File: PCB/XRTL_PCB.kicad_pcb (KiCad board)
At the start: 2 copper layers, 94 x 78.7 mm, 20 parts, among them J1 POWER, J10 servo1, J11 servo2, J12 infoLED, J2 stepper1, J3 stepper2, J4 ESP32 right, J5 ESP32 left, J6 relay1 IN, J7 relay2 IN, J8 relay1 OUT, J9 relay2 OUT, K1 TIANBO-HJR-4102-L, K2 TIANBO-HJR-4102-L, U1 TBD62003, U2 TBD62003

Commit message: Add files via upload
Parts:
- J6: value relay1 IN -> relay2 IN
- J7: value relay2 IN -> relay1 IN
- J8: value relay1 OUT -> relay2 OUT
- J9: value relay2 OUT -> relay1 OUT
- moved J11 90.9 mm to (132.1, 71.1), turned to 0 degrees
- moved J4 82.9 mm to (127.0, 127.0), turned to 180 degrees
- moved J5 82.9 mm to (101.6, 127.0), turned to 180 degrees
- moved J10 75.0 mm to (132.1, 61.0), turned to 0 degrees
- moved J2 69.1 mm to (81.3, 111.8)
- moved U1 69.1 mm to (96.5, 127.0)
- moved J12 58.0 mm to (129.5, 53.3)
- moved J1 55.6 mm to (81.3, 73.7)
- moved C1 48.5 mm to (86.4, 81.2), turned to 90 degrees
- moved C2 48.4 mm to (88.9, 106.1)
- moved D1 45.0 mm to (99.1, 73.7)
- moved J3 41.3 mm to (81.3, 91.4)
- moved U2 40.6 mm to (96.5, 99.1)
- moved J8 35.9 mm to (86.4, 53.3), turned to 180 degrees
- moved J6 28.8 mm to (99.1, 53.3), turned to 180 degrees
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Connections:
- D1 pad 2: driverRelay1 -> driverRelay2
- D2 pad 2: driverRelay2 -> driverRelay1
- J2 pad 1: Net-(U1-Pad13) -> Net-(J2-Pad1)
- J2 pad 2: Net-(U1-Pad14) -> Net-(J2-Pad2)
- J2 pad 3: Net-(U1-Pad15) -> Net-(U1-Pad12)
- J2 pad 4: Net-(U1-Pad16) -> Net-(U1-Pad13)
- J3 pad 1: Net-(U2-Pad10) -> Net-(J3-Pad1)
- J3 pad 2: Net-(U2-Pad11) -> Net-(J3-Pad2)
- J3 pad 3: Net-(U2-Pad12) -> Net-(J3-Pad3)
- J3 pad 4: Net-(U2-Pad13) -> Net-(U2-Pad16)
- J5 pad 10: stepper2B -> stepper2C
- J5 pad 11: stepper2C -> stepper2B
- J5 pad 12: stepper2D -> stepper2A
- J5 pad 2: stepper1A -> stepper1D
- J5 pad 3: stepper1B -> stepper1C
- J5 pad 6: stepper1C -> stepper1B
- J5 pad 8: stepper1D -> stepper1A
- J5 pad 9: stepper2A -> stepper2D
- K1 pad 8: driverRelay2 -> driverRelay1
- K2 pad 8: driverRelay1 -> driverRelay2
- U1 pad 1: stepper1D -> unconnected-(U1-Pad1)
- U1 pad 10: unconnected-(U1-Pad10) -> Net-(J2-Pad1)
- U1 pad 11: unconnected-(U1-Pad11) -> Net-(J2-Pad2)
- U1 pad 12: unconnected-(U1-Pad12) -> Net-(U1-Pad12)
- U1 pad 14: Net-(U1-Pad14) -> unconnected-(U1-Pad14)
- U1 pad 15: Net-(U1-Pad15) -> unconnected-(U1-Pad15)
- U1 pad 16: Net-(U1-Pad16) -> unconnected-(U1-Pad16)
- U1 pad 2: stepper1C -> unconnected-(U1-Pad2)
- U1 pad 3: stepper1B -> unconnected-(U1-Pad3)
- U1 pad 4: stepper1A -> stepper1D
- U1 pad 5: unconnected-(U1-Pad5) -> stepper1C
- U1 pad 6: unconnected-(U1-Pad6) -> stepper1B
- U1 pad 7: unconnected-(U1-Pad7) -> stepper1A
- U2 pad 1: relay1 -> stepper2D
- U2 pad 10: Net-(U2-Pad10) -> driverRelay1
- U2 pad 11: Net-(U2-Pad11) -> driverRelay2
- U2 pad 12: Net-(U2-Pad12) -> unconnected-(U2-Pad12)
- U2 pad 13: Net-(U2-Pad13) -> Net-(J3-Pad1)
- U2 pad 14: unconnected-(U2-Pad14) -> Net-(J3-Pad2)
- U2 pad 15: driverRelay2 -> Net-(J3-Pad3)
- U2 pad 16: driverRelay1 -> Net-(U2-Pad16)
- U2 pad 2: relay2 -> stepper2C
- U2 pad 3: unconnected-(U2-Pad3) -> stepper2B
- U2 pad 4: stepper2D -> stepper2A
- U2 pad 5: stepper2C -> unconnected-(U2-Pad5)
- U2 pad 6: stepper2B -> relay2
- U2 pad 7: stepper2A -> relay1
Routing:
- net +5V: track 385.6 -> 0.00 mm
- net GND: track 219.7 -> 0.00 mm
- net driverRelay1: track 117.8 -> 34.7 mm
- net driverRelay2: track 98.6 -> 18.8 mm
- net servo2: track 56.9 -> 32.6 mm
- net infoLED: track 41.3 -> 61.6 mm
- net Net-(J7-Pad2): track 32.1 -> 17.3 mm
- net Net-(J6-Pad2): track 32.0 -> 17.3 mm
- net Net-(U1-Pad16): track 10.9 -> 0.00 mm
- net Net-(U1-Pad15): track 10.9 -> 0.00 mm
- net Net-(U1-Pad14): track 10.8 -> 0.00 mm
- net relay2: track 41.4 -> 51.6 mm
- net Net-(J3-Pad3): track 0.00 -> 7.73 mm
- net Net-(J3-Pad2): track 0.00 -> 7.69 mm
- net Net-(J2-Pad2): track 0.00 -> 7.69 mm
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- added copper zone on F.Cu, net +5V
- added copper zone on B.Cu, net GND
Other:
- board size 94 x 78.7 mm -> 63.5 x 86.4 mm

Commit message: Add files via upload
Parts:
- removed J1: POWER, Connector_USB:USB_A_Stewart_SS-52100-001_Horizontal
- added C3: 100n, Capacitor_THT:C_Disc_D3.0mm_W1.6mm_P2.50mm, F.Cu at (127.0, 76.2)
- added J13: USBC_5V_3A_input, Connector_USB:USB_C_Receptacle_GCT_USB4085, F.Cu at (81.3, 71.1)
- added R1: 5.1k, Resistor_THT:R_Axial_DIN0204_L3.6mm_D1.6mm_P5.08mm_Horizontal, F.Cu at (81.3, 81.3)
- added R2: 5.1k, Resistor_THT:R_Axial_DIN0204_L3.6mm_D1.6mm_P5.08mm_Horizontal, F.Cu at (81.3, 66.0)
- C1, C2: footprint Capacitor_THT:C_Disc_D3.4mm_W2.1mm_P2.50mm -> Capacitor_THT:C_Disc_D3.0mm_W1.6mm_P2.50mm
- moved C2 30.0 mm to (91.4, 76.2)
- moved C1 23.5 mm to (91.4, 104.1), turned to 0 degrees
- moved D1 11.4 mm to (104.1, 63.5), turned to -90 degrees
- moved D2 5.08 mm to (119.4, 73.7)
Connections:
- J4 pad 11: unconnected-(J4-Pad11) -> relay1
- J4 pad 15: relay1 -> unconnected-(J4-Pad15)
- K1 pad 1: (no net) -> Net-(J7-Pad2)
- K2 pad 1: (no net) -> Net-(J6-Pad2)
- U2 pad 10: driverRelay1 -> driverRelay2
- U2 pad 11: driverRelay2 -> driverRelay1
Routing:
- net +5V: track 0.00 -> 276.9 mm
- net driverRelay2: track 18.8 -> 36.8 mm
- net relay1: track 38.1 -> 48.0 mm
- net Net-(J13-PadB5): track 0.00 -> 8.32 mm
- net Net-(J13-PadA5): track 0.00 -> 7.73 mm
- net GND: track 0.00 -> 2.70 mm, vias 0 -> 18
- net driverRelay1: track 34.7 -> 32.8 mm
- added copper zone on F.Cu, net GND
- removed copper zone on F.Cu, net +5V
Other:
- board text added: "+"
- board text added: "-"
- board text added: "1A"
- board text added: "1B"
- board text added: "1C"
- board text added: "1D"
- board text added: "2A"
- board text added: "2B"
- board text added: "2C"
- board text added: "2D"
- board text added: "3V3"
- board text added: "5V"
- board text added: "GND"
- board text added: "IN"
- board text added: "LED"
- board text added: "OUT"
- board text added: "POWER"
- board text added: "XRTL v1.0 Jari Domke 23/05/2022"
- board text added: "infoLED"
- board text added: "relay1"
- board text added: "relay2"
- board text added: "servo1"
- board text added: "servo2"
- board text added: "stepper1"
- board text added: "stepper2"

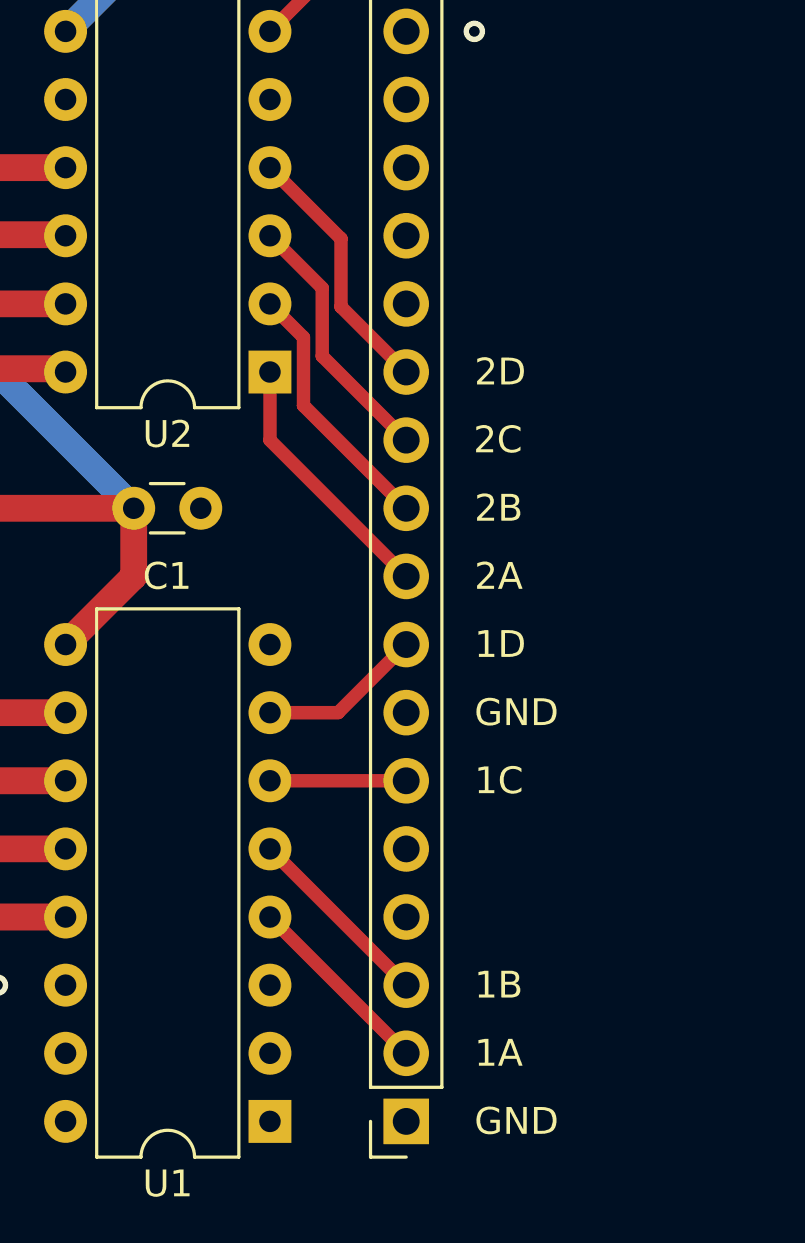
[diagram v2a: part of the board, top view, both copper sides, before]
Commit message: Add files via upload
fixed pin assignment
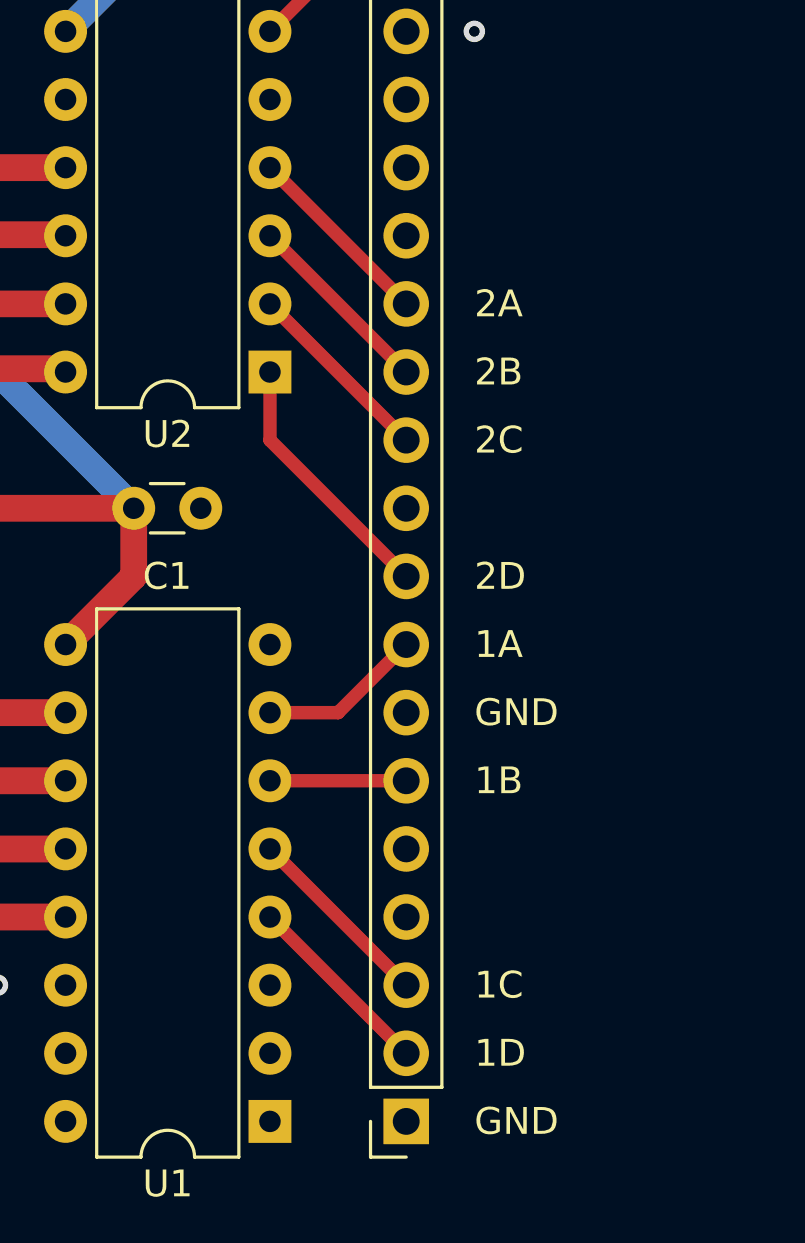
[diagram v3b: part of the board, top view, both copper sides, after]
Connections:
- J5 pad 10: stepper2C -> unconnected-(J5-Pad10)
- J5 pad 11: stepper2B -> stepper2C
- J5 pad 12: stepper2A -> stepper2B
- J5 pad 13: unconnected-(J5-Pad13) -> stepper2A
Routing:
- net stepper2C: track 9.72 -> 7.18 mm
- net stepper2A: track 9.72 -> 7.18 mm
- net stepper2B: track 9.72 -> 7.18 mm
